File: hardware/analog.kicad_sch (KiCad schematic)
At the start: 15 parts, among them J1 Conn_01x02, U1 ${SIM.PARAMS}, U2 ${SIM.PARAMS}, U3 ${SIM.PARAMS}, U4 ADG621BRMZ

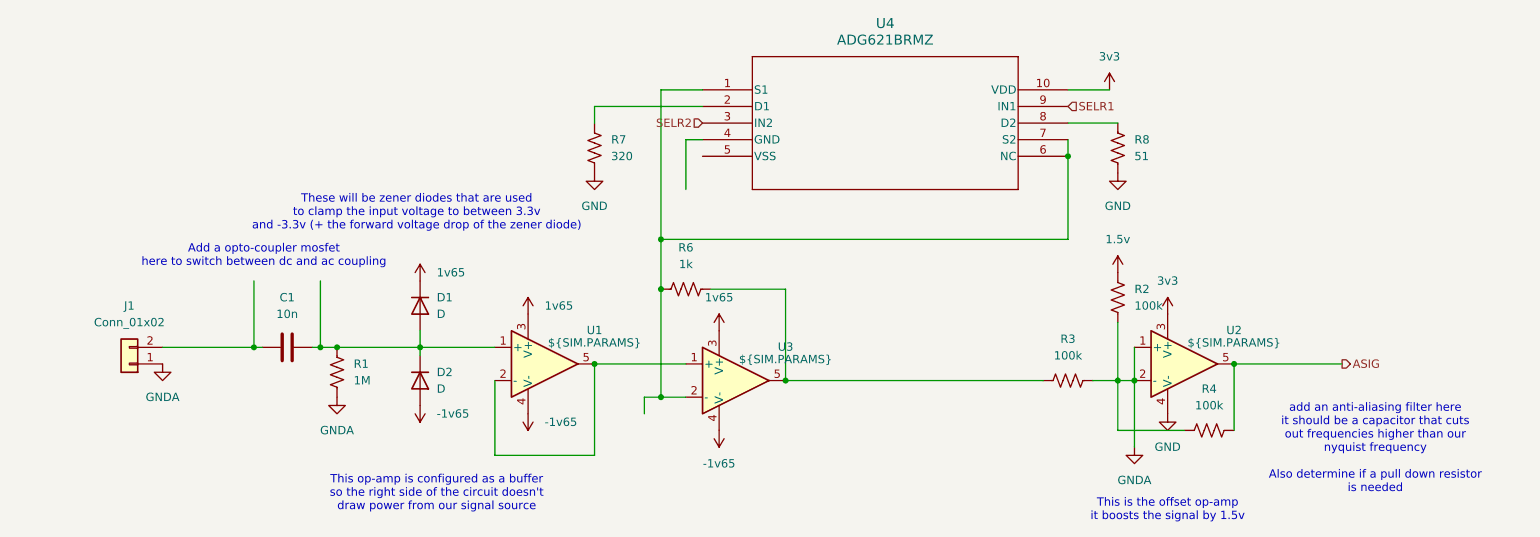
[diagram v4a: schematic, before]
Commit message: finished part selection for analog/added photorelay switch for ac/dc coupling
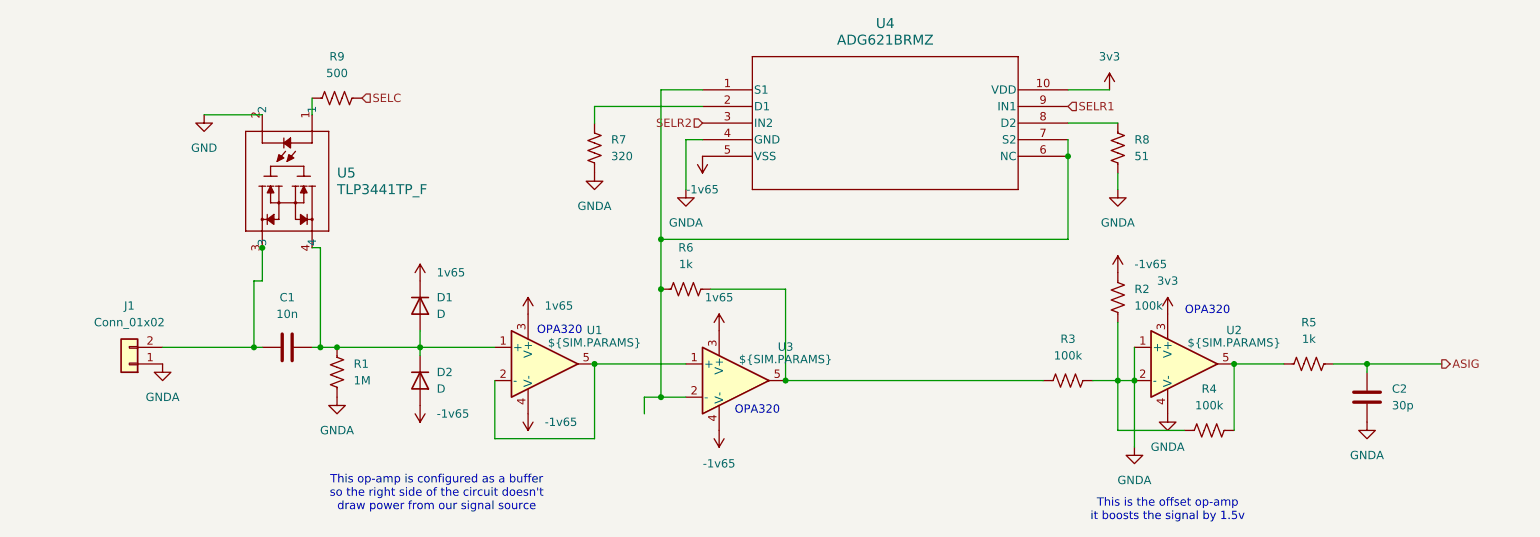
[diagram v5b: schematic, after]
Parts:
- added C2: 30p, symbol Device:C
- added R5: 1k, symbol Device:R_US
- added R9: 500, symbol Device:R_US
- added U5: TLP3441TP_F, VSON4_TOS, symbol TLP3441:TLP3441TP_F
- C1: Purchase Link (none) -> https://www.digikey.com/en/products/detail/kemet/C0603X103J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
- D1, D2: Purchase Link (none) -> https://www.digikey.com/en/products/detail/onsemi/BAT54T1G/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
- R1: Purchase Link (none) -> https://www.digikey.com/en/products/detail/te-connectivity-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
- R2, R3, R4: Purchase Link (none) -> https://www.digikey.com/en/products/detail/susumu/RG2012P-1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
- R6, R8: Purchase Link (none) -> https://www.digikey.com/en/products/detail/panasonic-electr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
- R7: Purchase Link (none) -> https://www.digikey.com/en/products/detail/vishay-dale/TNPW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
- U3: Purchase Link (none) -> https://www.digikey.com/en/products/detail/texas-instrument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
- U4: Purchase Link (none) -> https://www.digikey.com/en/products/detail/analog-devices-i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
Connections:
- net 1.5v is gone; now on net -1v65: R2.2
- net -1v65: now also U4.5 (VSS)
- net ASIG: now also C2.1, R5.2; no longer R4.1, U2.5
- net GND: no longer R7.1, R8.1, U2.4 (V-)
- net GNDA: now also R7.1, R8.1, U2.4 (V-), U4.4 (GND), C2.2
- net at C1.1, J1.2 (Pin_2): now also U5.3
- new net: R4.1, R5.1, U2.5
- new net SELC: R9.2
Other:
- note added: "OPA320"
- note removed: "Add a opto-coupler mosfet here to switch between dc and ac coupling"
- note removed: "These will be zener diodes that are used to clamp the input voltage to between 3.3v and -3.3v (+ the forward voltage drop of the zener diode)"
- note removed: "add an anti-aliasing filter here it should be a capacitor that cuts out frequencies higher than our nyquist frequency Also determine if a pull down resistor is needed"

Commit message: Up to date
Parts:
- renumbered C2 to C?, C1 to C?, D1 to D?, D2 to D?, J1 to J?, R7 to R?, R9 to R?, R6 to R?, R2 to R?, R4 to R?, R3 to R?, R1 to R?, R8 to R?, R5 to R?, U1 to U?, U3 to U?, U2 to U?, U5 to U?, U4 to U?

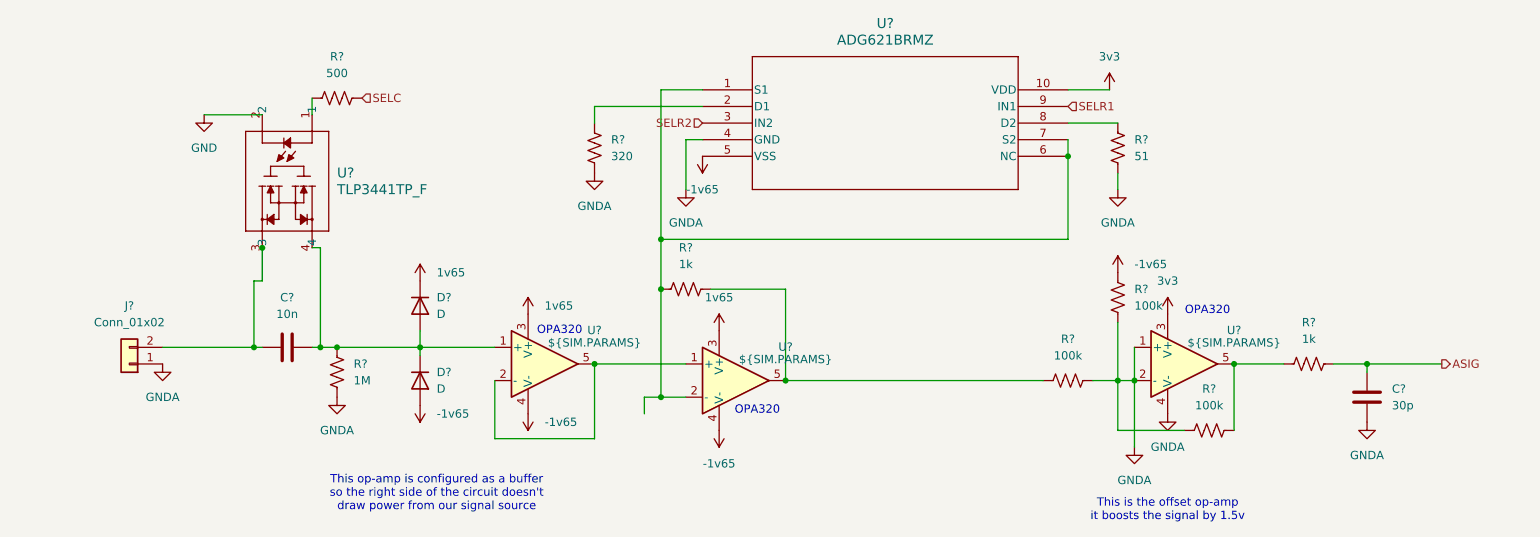
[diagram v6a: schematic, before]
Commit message: added bnc foorptint and symbol
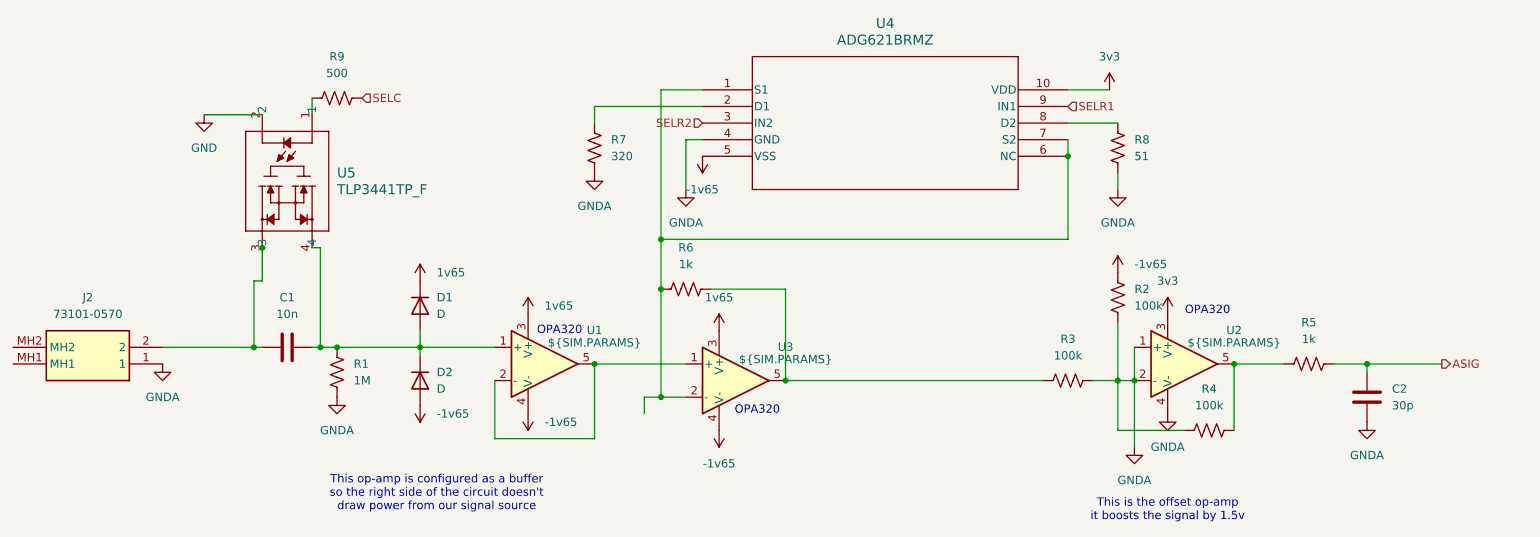
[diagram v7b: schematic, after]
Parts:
- removed J?: Conn_01x02, symbol Connector_Generic:Conn_01x02
- added J2: 73101-0570, 731010570, symbol BNC:73101-0570
- gave numbers to parts that had none: 18
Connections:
- net GNDA: now also J2.1
- net at C1.1, U5.3: now also J2.2

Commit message: Trig finished
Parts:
- renumbered C2 to C?, C1 to C?, D1 to D?, D2 to D?, J2 to J?, R7 to R?, R9 to R?, R6 to R?, R2 to R?, R4 to R?, R3 to R?, R1 to R?, R8 to R?, R5 to R?, U1 to U?, U3 to U?, U2 to U?, U5 to U?, U4 to U?
